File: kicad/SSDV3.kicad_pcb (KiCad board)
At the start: 4 copper layers, 58.4 x 28.8 mm, 72 parts, among them J1 SolderPad, J2 SolderPad, J3 SolderPad, J4 SolderPad, J5 SolderPad, J6 SolderPad, J7 SolderPad_01x02, J8 SolderPad_1x03, Q1 CSD19537Q3, Q2 CSD19537Q3, Q3 BSZ096N10LS5, U1 LM5050-1, U2 LM5146RGYR

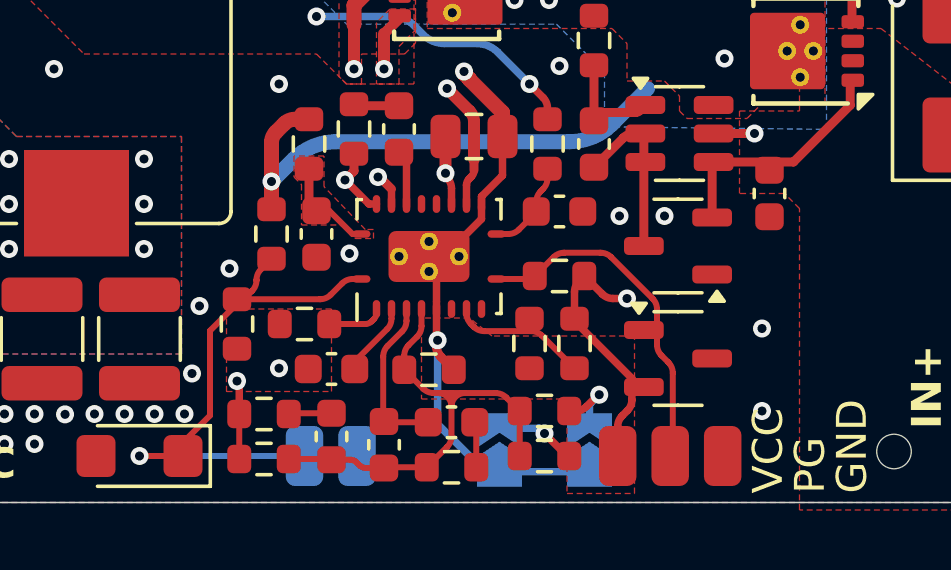
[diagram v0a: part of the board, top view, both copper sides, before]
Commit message: Improved LM5146 footprint
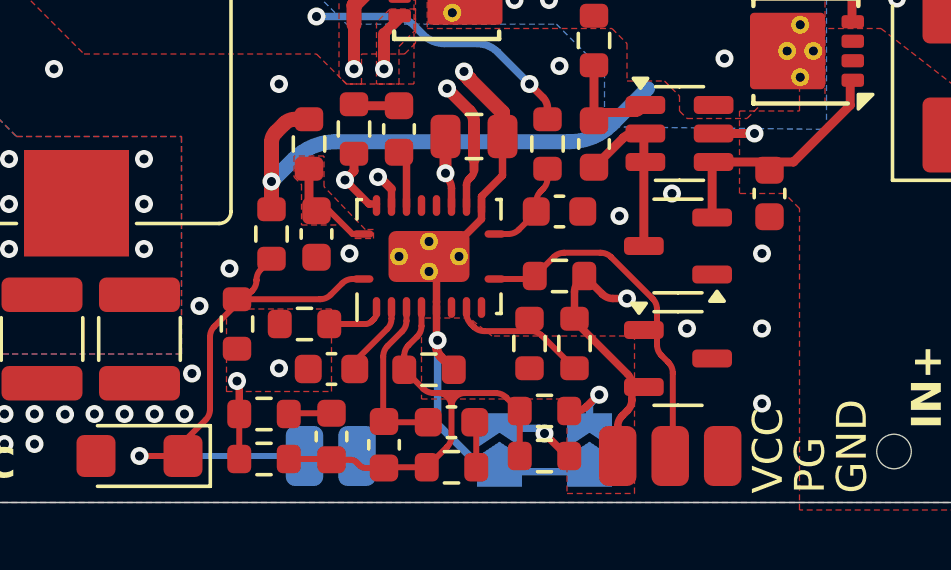
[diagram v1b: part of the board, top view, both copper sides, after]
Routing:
- net PGND: vias 114 -> 116
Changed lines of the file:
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@@
 		(layer "F.Cu")
 		(at 154.4 120.6 90)
-		(descr "20 Pin VQFN (https://www.ti.com/lit/pdf/mpqf116h) by Julian Joaquin")
+		(descr "20 Pin VQFN (https://www.ti.com/lit/pdf/mpqf116h) created using QFN script by Julian Joaquin")
 		(tags "VQFN LM5145 LM5146")
 		(property "Reference" "U2"
@@
 		)
 		(pad "1" smd oval
-			(at -0.75 -2.25 90)
-			(size 0.25 0.6)
+			(at -0.75 -2.2 90)
+			(size 0.25 0.7)
 			(layers "F.Cu" "F.Mask" "F.Paste")
 			(net 23 "U1_EN")
@@
 		)
 		(pad "2" smd oval
-			(at -1.75 -1.75 180)
-			(size 0.25 0.6)
+			(at -1.7 -1.75 180)
+			(size 0.25 0.7)
 			(layers "F.Cu" "F.Mask" "F.Paste")
 			(net 18 "/RT")
@@
 		)
 		(pad "3" smd oval
-			(at -1.75 -1.25 180)
-			(size 0.25 0.6)
+			(at -1.7 -1.25 180)
+			(size 0.25 0.7)
 			(layers "F.Cu" "F.Mask" "F.Paste")
 			(net 4 "/SS_TRK")
@@
 		)
 		(pad "4" smd oval
-			(at -1.75 -0.75 180)
-			(size 0.25 0.6)
+			(at -1.7 -0.75 180)
+			(size 0.25 0.7)
 			(layers "F.Cu" "F.Mask" "F.Paste")
 			(net 9 "/COMP")
@@
 		)
 		(pad "5" smd oval
-			(at -1.75 -0.25 180)
-			(size 0.25 0.6)
+			(at -1.7 -0.25 180)
+			(size 0.25 0.7)
 			(layers "F.Cu" "F.Mask" "F.Paste")
 			(net 7 "/FB")
@@
 		)
 		(pad "6" smd oval
-			(at -1.75 0.25 180)
-			(size 0.25 0.6)
+			(at -1.7 0.25 180)
+			(size 0.25 0.7)
 			(layers "F.Cu" "F.Mask" "F.Paste")
 			(net 2 "AGND")
@@
 		)
 		(pad "7" smd oval
-			(at -1.75 0.75 180)
-			(size 0.25 0.6)
+			(at -1.7 0.75 180)
+			(size 0.25 0.7)
 			(layers "F.Cu" "F.Mask" "F.Paste")
 			(net 30 "unconnected-(U2-SYNCOUT-Pad7)")
@@
 		)
 		(pad "8" smd oval
-			(at -1.75 1.25 180)
-			(size 0.25 0.6)
+			(at -1.7 1.25 180)
+			(size 0.25 0.7)
 			(layers "F.Cu" "F.Mask" "F.Paste")
 			(net 12 "/SYNCIN")
@@
 		)
 		(pad "9" smd oval
-			(at -1.75 1.75 180)
-			(size 0.25 0.6)
+			(at -1.7 1.75 180)
+			(size 0.25 0.7)
 			(layers "F.Cu" "F.Mask" "F.Paste")
 			(net 31 "unconnected-(U2-NC-Pad9)")
@@
 		)
 		(pad "10" smd oval
-			(at -0.75 2.25 90)
-			(size 0.25 0.6)
+			(at -0.75 2.2 90)
+			(size 0.25 0.7)
 			(layers "F.Cu" "F.Mask" "F.Paste")
 			(net 15 "PG")
@@
 		)
 		(pad "11" smd oval
-			(at 0.75 2.25 90)
-			(size 0.25 0.6)
+			(at 0.75 2.2 90)
+			(size 0.25 0.7)
 			(layers "F.Cu" "F.Mask" "F.Paste")
 			(net 6 "/ILIM")
@@
 		)
 		(pad "12" smd oval
-			(at 1.75 1.75 180)
-			(size 0.25 0.6)
+			(at 1.7 1.75 180)
+			(size 0.25 0.7)
 			(layers "F.Cu" "F.Mask" "F.Paste")
 			(net 1 "PGND")
@@
 		)
 		(pad "13" smd oval
-			(at 1.75 1.25 180)
-			(size 0.25 0.6)
+			(at 1.7 1.25 180)
+			(size 0.25 0.7)
 			(layers "F.Cu" "F.Mask" "F.Paste")
 			(net 16 "/LO")
@@
 		)
 		(pad "14" smd oval
-			(at 1.75 0.75 180)
-			(size 0.25 0.6)
+			(at 1.7 0.75 180)
+			(size 0.25 0.7)
 			(layers "F.Cu" "F.Mask" "F.Paste")
 			(net 3 "VCC")
@@
 		)
 		(pad "15" smd oval
-			(at 1.75 0.25 180)
-			(size 0.25 0.6)
+			(at 1.7 0.25 180)
+			(size 0.25 0.7)
 			(layers "F.Cu" "F.Mask" "F.Paste")
 			(net 1 "PGND")
@@
 		)
 		(pad "16" smd oval
-			(at 1.75 -0.25 180)
-			(size 0.25 0.6)
+			(at 1.7 -0.25 180)
+			(size 0.25 0.7)
 			(layers "F.Cu" "F.Mask" "F.Paste")
 			(net 1 "PGND")
@@
 		)
 		(pad "17" smd oval
-			(at 1.75 -0.75 180)
-			(size 0.25 0.6)
+			(at 1.7 -0.75 180)
+			(size 0.25 0.7)
 			(layers "F.Cu" "F.Mask" "F.Paste")
 			(net 5 "/BST")
@@
 		)
 		(pad "18" smd oval
-			(at 1.75 -1.25 180)
-			(size 0.25 0.6)
+			(at 1.7 -1.25 180)
+			(size 0.25 0.7)
 			(layers "F.Cu" "F.Mask" "F.Paste")
 			(net 13 "/HO")
@@
 		)
 		(pad "19" smd oval
-			(at 1.75 -1.75 180)
-			(size 0.25 0.6)
+			(at 1.7 -1.75 180)
+			(size 0.25 0.7)
 			(layers "F.Cu" "F.Mask" "F.Paste")
 			(net 14 "/SW")
@@
 		)
 		(pad "20" smd oval
-			(at 0.75 -2.25 90)
-			(size 0.25 0.6)
+			(at 0.75 -2.2 90)
+			(size 0.25 0.7)
 			(layers "F.Cu" "F.Mask" "F.Paste")
 			(net 28 "/U2_VIN")
@@
 	)
 	(via
-		(at 165.5 125.75)
+		(at 165.5 125.5)
 		(size 0.6)
 		(drill 0.3)
@@
 	)
 	(via
-		(at 162.25 119.25)
+		(at 163 123)
+		(size 0.6)
+		(drill 0.3)
+		(layers "F.Cu" "B.Cu")
+		(free yes)
+		(net 1)
+	)
+	(via
+		(at 162.5 118.5)
 		(size 0.6)
 		(drill 0.3)
@@
 	)
 	(via
+		(at 165.5 120.5)
+		(size 0.6)
+		(drill 0.3)
+		(layers "F.Cu" "B.Cu")
+		(free yes)
+		(net 1)
+	)
+	(via
 		(at 135.4 107.85)
 		(size 0.6)
@@
 	)
 	(segment
-		(start 161.1625 124.6625)
+		(start 161.016053 124.516053)
 		(end 159.25 122.75)
 		(width 0.25)
@@
 	)
 	(segment
-		(start 161.1625 124.6625)
+		(start 161.1625 124.869607)
 		(end 161.1625 125.380393)
 		(width 0.25)
@@
 		(net 3)
 	)
+	(arc
+		(start 161.016053 124.516053)
+		(mid 161.12444 124.678265)
+		(end 161.1625 124.869607)
+		(width 0.25)
+		(layer "F.Cu")
+		(net 3)
+	)
 	(segment
 		(start 160.25 122)
@@
 	)
 	(segment
-		(start 147.1 125.9)
+		(start 146.953553 126.046447)
 		(end 146.2 126.8)
 		(width 0.2)
@@
 	)
 	(segment
-		(start 147.1 123.075)
-		(end 147.1 125.9)
+		(start 147.1 123.282107)
+		(end 147.1 125.692893)
 		(width 0.2)
 		(layer "F.Cu")
@@
 	(segment
 		(start 148.15 122.025)
-		(end 147.1 123.075)
+		(end 147.246446 122.928554)
 		(width 0.2)
 		(layer "F.Cu")
@@
 	)
 	(arc
+		(start 147.1 125.692893)
+		(mid 147.06194 125.884235)
+		(end 146.953553 126.046447)
+		(width 0.2)
+		(layer "F.Cu")
+		(net 23)
+	)
+	(arc
 		(start 148.796447 121.028553)
 		(mid 148.68806 121.190765)
@@
 		(width 0.2)
 		(layer "F.Cu")
+		(net 23)
+	)
+	(arc
+		(start 147.1 123.282107)
+		(mid 147.13806 123.090766)
+		(end 147.246446 122.928554)
+		(width 0.2)
+		(layer "F.Cu")

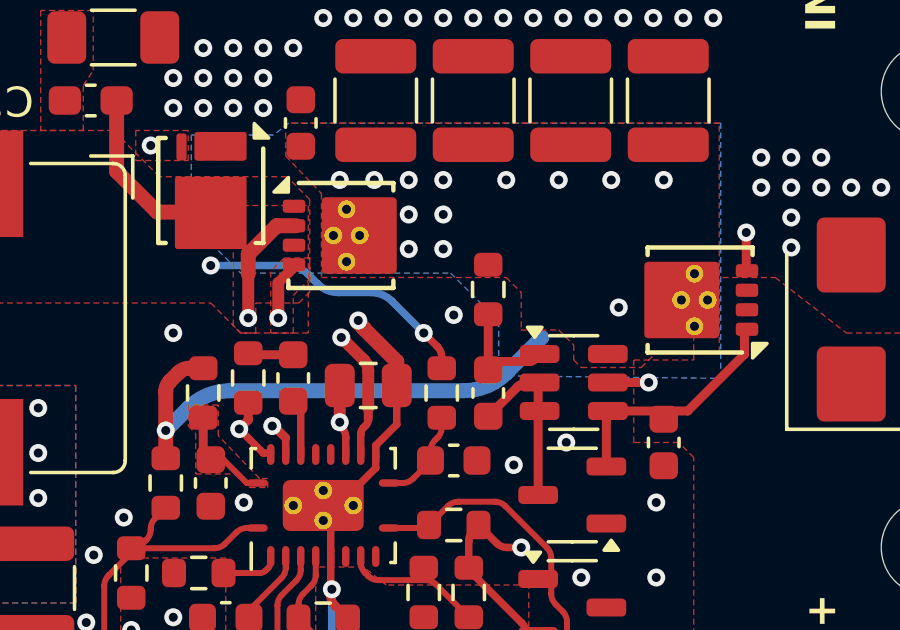
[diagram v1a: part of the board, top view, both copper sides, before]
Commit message: Added schematic details, added license, improved README
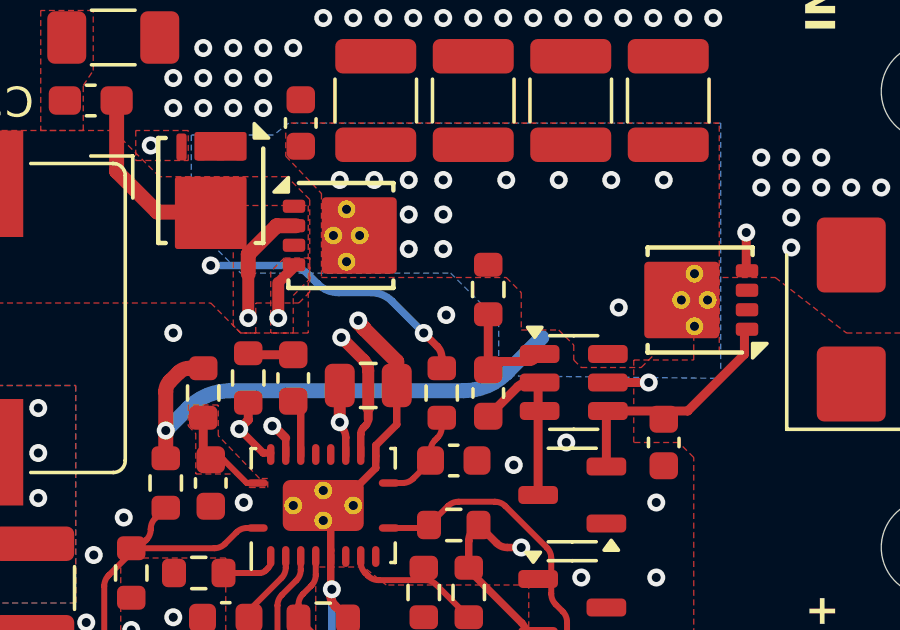
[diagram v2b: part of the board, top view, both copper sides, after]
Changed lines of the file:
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@@
 		(date "2025-10-20")
 		(rev "C")
-		(company "UBCO Aerospace [Julian Joaquin]")
+		(company "Julian Joaquin")
 		(comment 1 "A 12S battery eliminator circuit (BEC) for UAS applications.")
 	)
@@
 			)
 		)
+		(property "Qg" "18nC"
+			(at 0 0 270)
+			(unlocked yes)
+			(layer "F.Fab")
+			(hide yes)
+			(effects
+				(font
+					(size 1 1)
+					(thickness 0.15)
+				)
+			)
+		)
+		(property "Qoss" "30nC"
+			(at 0 0 270)
+			(unlocked yes)
+			(layer "F.Fab")
+			(hide yes)
+			(effects
+				(font
+					(size 1 1)
+					(thickness 0.15)
+				)
+			)
+		)
+		(property "Qrr" "34nC"
+			(at 0 0 270)
+			(unlocked yes)
+			(layer "F.Fab")
+			(hide yes)
+			(effects
+				(font
+					(size 1 1)
+					(thickness 0.15)
+				)
+			)
+		)
 		(property ki_fp_filters "VSON*3.3x3.3mm*P0.65mm*NexFET*")
 		(sheetname "/")
@@
 			)
 		)
-		(property "MANUFACTURER" "KEMET"
-			(at 0 0 90)
-			(unlocked yes)
-			(layer "F.Fab")
-			(hide yes)
-			(effects
-				(font
-					(size 1 1)
-					(thickness 0.15)
-				)
-			)
-		)
 		(property "Part Number" "T521D107M025ATE040"
 			(at 0 0 90)
@@
 		)
 		(embedded_fonts no)
-		(model "${KICAD9_3DMODEL_DIR}/Capacitor_Tantalum_SMD.3dshapes/CP_EIA-7343-20_Kemet-V.step"
+		(model "${KIPRJMOD}/lib/SnapMagic/sm_T521D107M025ATE040/T521D107M025ATE040.STEP"
+			(hide yes)
+			(offset
+				(xyz 0 0 0)
+			)
+			(scale
+				(xyz 1 1 1)
+			)
+			(rotate
+				(xyz -90 -0 -0)
+			)
+		)
+		(model "${KICAD9_3DMODEL_DIR}/Capacitor_Tantalum_SMD.3dshapes/CP_EIA-7343-31_Kemet-D.step"
 			(offset
 				(xyz 0 0 0)
@@
 			)
 		)
+		(property "Qg" "12nC"
+			(at 0 0 0)
+			(unlocked yes)
+			(layer "F.Fab")
+			(hide yes)
+			(effects
+				(font
+					(size 1 1)
+					(thickness 0.15)
+				)
+			)
+		)
+		(property "Rds(on)" "12.1mΩ"
+			(at 0 0 0)
+			(unlocked yes)
+			(layer "F.Fab")
+			(hide yes)
+			(effects
+				(font
+					(size 1 1)
+					(thickness 0.15)
+				)
+			)
+		)
 		(property ki_fp_filters "VSON*3.3x3.3mm*P0.65mm*NexFET*")
 		(sheetname "/")
@@
 	)
 	(via
-		(at 158.75 114.25)
+		(at 158.5 114.25)
 		(size 0.6)
 		(drill 0.3)

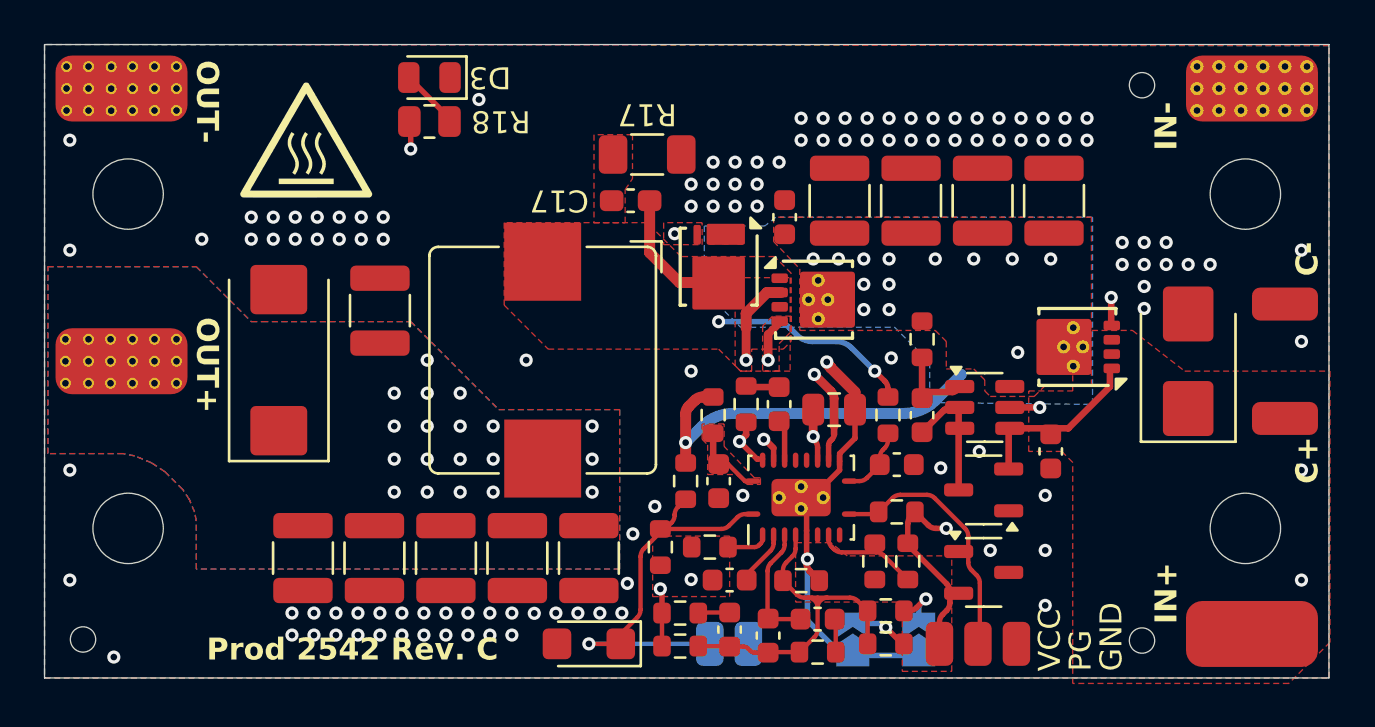
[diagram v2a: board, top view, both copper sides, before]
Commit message: revD started, fixed reverse polarity issues and improve temp rating
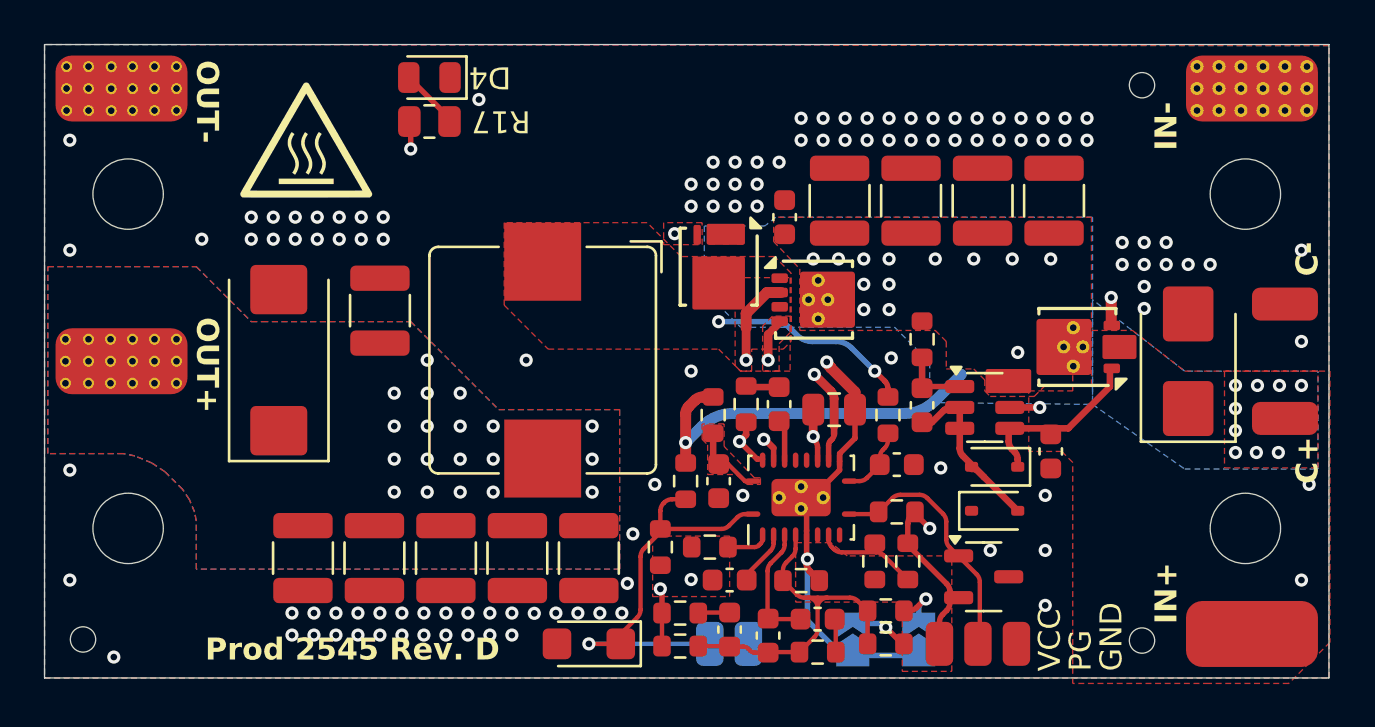
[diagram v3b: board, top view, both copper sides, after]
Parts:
- removed the C17 at (146.7, 107.1)
- removed the R17 at (147.4, 105.0)
- added D3: BAT46WS, Diode_SMD:D_SOD-323, F.Cu at (163.2, 121.2)
- D2: value BAS70-06 -> BAT46WS; footprint Package_TO_SOT_SMD:SOT-23-3 -> Diode_SMD:D_SOD-323
- D4: renamed from D3; value YELLOW -> GREEN
- moved D2 1.16 mm to (163.2, 119.2)
- moved C3 0.45 mm to (159.9, 116.4)
- moved D6 0.20 mm to (162.7, 124.2)
- renumbered C14 to C12, C15 to C13, C16 to C14, C12 to C15, C13 to C16, C18 to C17, C19 to C18, C20 to C19, C21 to C20, C22 to C21, C23 to C22, C24 to C23, D4 to D5, D5 to D6, R12 to R10, R13 to R11, R14 to R12, R15 to R13, R16 to R14, R9 to R15, R10 to R16, R18 to R17, R11 to R9
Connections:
- D2 pad 1: PGND -> VBAT
- D2 pad 2: VBAT -> /U1_GND
- J2 pad 1: VBAT -> VIN
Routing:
- net /SW: track 25.7 -> 19.6 mm
- net /U1_GND: track 5.52 -> 8.09 mm
- net VCC: track 18.9 -> 17.1 mm
- net U1_EN: track 18.5 -> 19.1 mm
- net VIN: vias 14 -> 23
- net PGND: vias 116 -> 115
- added copper zone on In1.Cu, net VIN
- removed copper zone on F.Cu, net /SNUB_RC
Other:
- board text added: "Prod 2545 Rev. D"
- board text added: "Prod 2545 Rev. D Julian Joaquin"
- board text removed: "Prod 2542 Rev. C"
- board text removed: "Prod 2542 Rev. C Julian Joaquin"
